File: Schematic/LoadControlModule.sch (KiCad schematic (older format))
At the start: 34 parts, among them Q1 IRF4905, Q10 2N3906, Q11 2N3906, Q12 IRF4905, Q13 2N3904, Q2 2N3904, Q3 IRF4905, Q4 2N3906, Q5 2N3906, Q6 IRF4905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

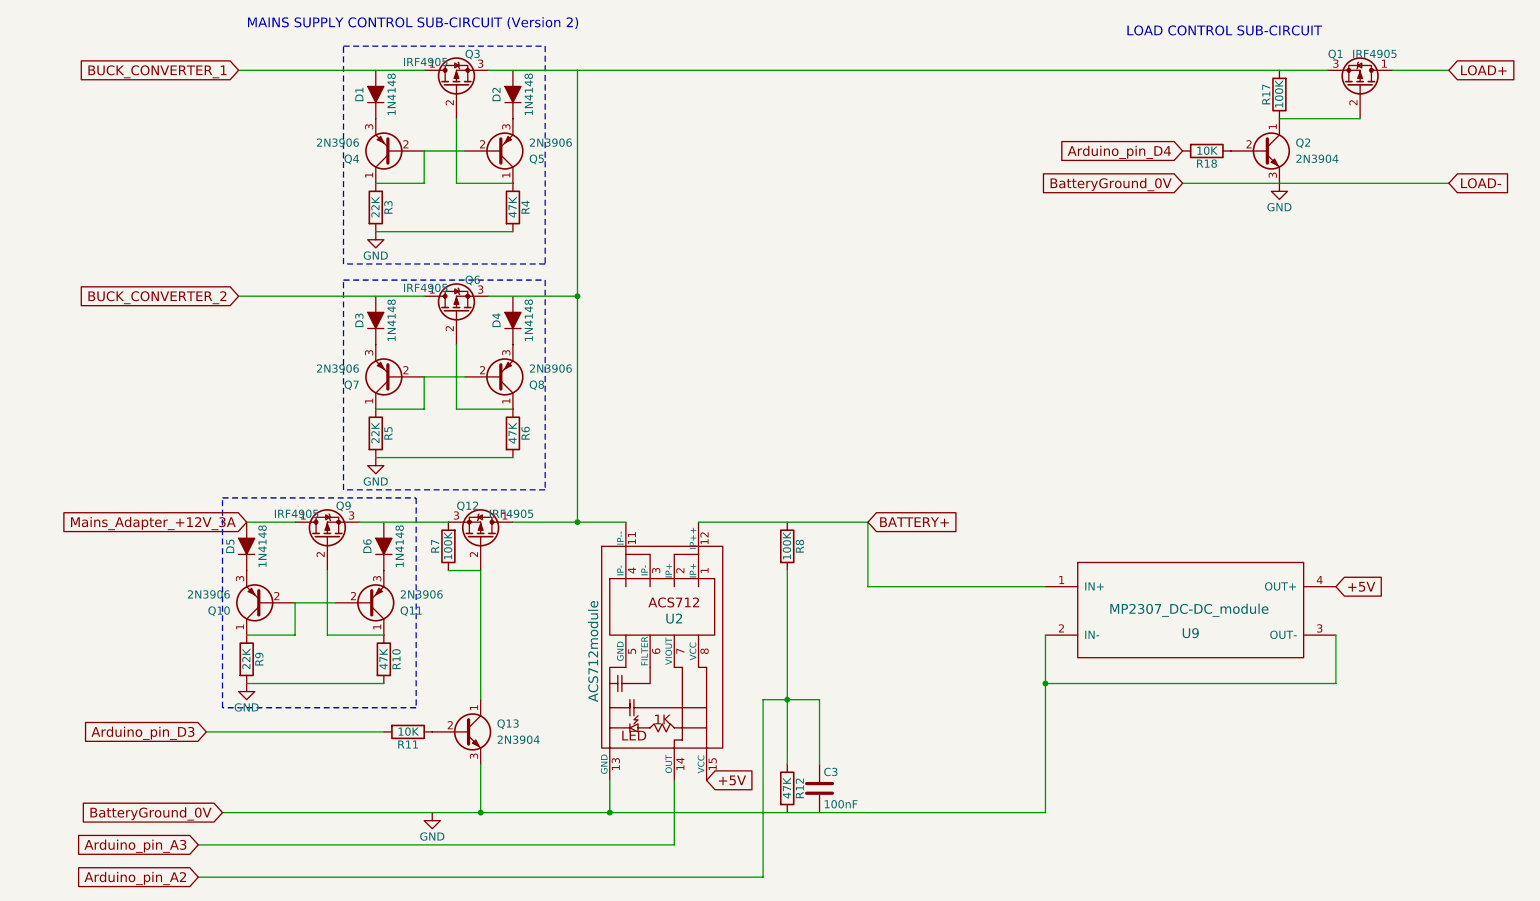
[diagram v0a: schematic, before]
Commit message: added BOM, started Fritzing prototype diagram, minor layout changes in KiCad
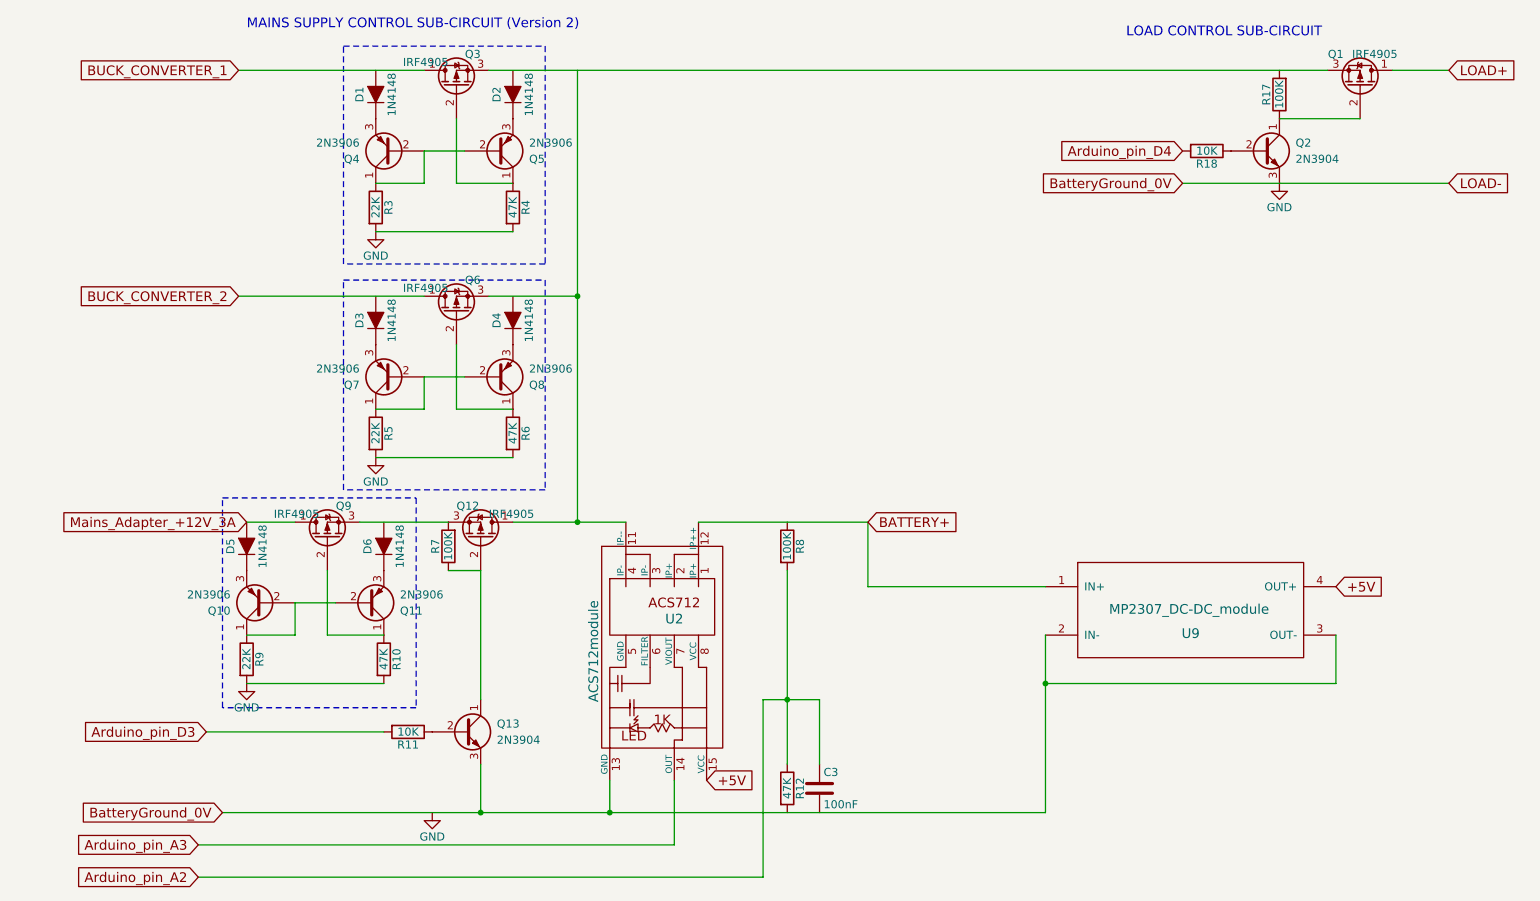
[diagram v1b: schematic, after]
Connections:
- net at Q12.1 (D), Q6.3 (S), U2.11 (IP--): no longer Q1.3 (S), Q3.3 (S)
- new net: Q1.3 (S), Q3.3 (S)
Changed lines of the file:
@@
 $EndComp
 Wire Wire Line
-	4100 1350 8750 1350
+	3550 1350 8750 1350
 Wire Wire Line
 	9150 1350 9500 1350
@@
 	7850 2050 9500 2050
 $Comp
-L GND #PWR10
+L GND #PWR010
 U 1 1 5AC48198
 P 8450 2050
-F 0 "#PWR10" H 8450 1800 50  0001 C CNN
+F 0 "#PWR010" H 8450 1800 50  0001 C CNN
 F 1 "GND" H 8450 1900 50  0000 C CNN
 F 2 "" H 8450 2050 50  0001 C CNN
@@
 $EndComp
 Wire Wire Line
-	7000 5950 5900 5950
-Wire Wire Line
-	5900 5950 4300 5950
-Wire Wire Line
-	4300 5950 3500 5950
-Wire Wire Line
-	3500 5950 1900 5950
-$Comp
-L GND #PWR14
+	7000 5950 1900 5950
+$Comp
+L GND #PWR011
 U 1 1 5AC61C7A
 P 3200 5950
-F 0 "#PWR14" H 3200 5700 50  0001 C CNN
+F 0 "#PWR011" H 3200 5700 50  0001 C CNN
 F 1 "GND" H 3200 5800 50  0000 C CNN
 F 2 "" H 3200 5950 50  0001 C CNN
@@
 	4850 4150 5900 4150
 Wire Wire Line
-	4100 1350 4100 2750
-Wire Wire Line
-	4100 2750 4100 4150
+	4100 1350 4100 4150
 Wire Wire Line
 	3500 4450 3300 4450
@@
 	2000 2750 3150 2750
 $Comp
-L GND #PWR12
+L GND #PWR012
 U 1 1 5AC61CA9
 P 2850 3750
-F 0 "#PWR12" H 2850 3500 50  0001 C CNN
+F 0 "#PWR012" H 2850 3500 50  0001 C CNN
 F 1 "GND" H 2850 3600 50  0000 C CNN
 F 2 "" H 2850 3750 50  0001 C CNN
@@
 	2050 4150 2350 4150
 $Comp
-L GND #PWR13
+L GND #PWR013
 U 1 1 5AC63545
 P 2050 5150
-F 0 "#PWR13" H 2050 4900 50  0001 C CNN
+F 0 "#PWR013" H 2050 4900 50  0001 C CNN
 F 1 "GND" H 2050 5000 50  0000 C CNN
 F 2 "" H 2050 5150 50  0001 C CNN
@@
 $EndComp
 Wire Wire Line
-	3550 1350 4100 1350
-Wire Wire Line
 	2000 1350 3150 1350
 $Comp
-L GND #PWR11
+L GND #PWR014
 U 1 1 5AC6C522
 P 2850 2350
-F 0 "#PWR11" H 2850 2100 50  0001 C CNN
+F 0 "#PWR014" H 2850 2100 50  0001 C CNN
 F 1 "GND" H 2850 2200 50  0000 C CNN
 F 2 "" H 2850 2350 50  0001 C CNN
@@
 	1900 5300 1900 4000
 Wire Wire Line
-	3700 4150 4100 4150
-Wire Wire Line
-	4100 4150 4400 4150
+	3700 4150 4400 4150
 $Comp
 L ACS712module U2
@@
 $EndComp
 Wire Wire Line
-	5400 4450 5400 5250
-Wire Wire Line
-	5400 5250 5400 5650
+	5400 4450 5400 5650
 Wire Wire Line
 	4300 5750 4300 5950
@@
 $EndComp
 Wire Wire Line
-	7000 4850 7000 5150
-Wire Wire Line
-	7000 5150 7000 5950
+	7000 4850 7000 5950
 Wire Wire Line
 	5900 4550 7000 4550
@@
 	5250 6350 5250 5250
 Wire Wire Line
-	5250 5250 5400 5250
-Wire Wire Line
-	5400 5250 5600 5250
+	5250 5250 5600 5250
 Connection ~ 5400 5250
 $Comp

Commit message: minor text changes
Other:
- note added: "MAINS SUPPLY CONTROL SUB-CIRCUIT"
- note added: "SOLAR CONVERTER CONNECTION SUB-CIRCUIT"
- note removed: "MAINS SUPPLY CONTROL SUB-CIRCUIT (Version 2)"
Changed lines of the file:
@@
 Wire Wire Line
 	3500 5250 3500 4450
-Text Notes 2050 1100 0    60   ~ 0
-MAINS SUPPLY CONTROL SUB-CIRCUIT (Version 2)
+Text Notes 600  3950 0    60   ~ 0
+MAINS SUPPLY CONTROL SUB-CIRCUIT
 $Comp
 L Q_PMOS_DGS Q12
@@
 Text GLabel 5900 4150 2    60   Input ~ 0
 BATTERY+
+Text Notes 1450 1100 0    60   ~ 0
+SOLAR CONVERTER CONNECTION SUB-CIRCUIT
 $EndSCHEMATC

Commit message: Minor corrections. Combined 3 sheets into a single schematic
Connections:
- net BatteryGround_0V is gone; now on net GND: Q13.3 (E), U2.13 (GND), U9.2 (IN-), U9.3 (OUT-)
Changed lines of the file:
@@
 Sheet 3 4
 Title "XL4016X2"
-Date "2018-04-06"
-Rev "V3"
+Date "2018-04-11"
+Rev "V3 minor corrections"
 Comp "farmerkeith"
 Comment1 ""
@@
 Text Notes 1450 1100 0    60   ~ 0
 SOLAR CONVERTER CONNECTION SUB-CIRCUIT
+Connection ~ 8450 2050
 $EndSCHEMATC
